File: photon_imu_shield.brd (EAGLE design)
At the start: 35.6 x 35.6 mm, 30 parts, among them U1 LSM9DS1

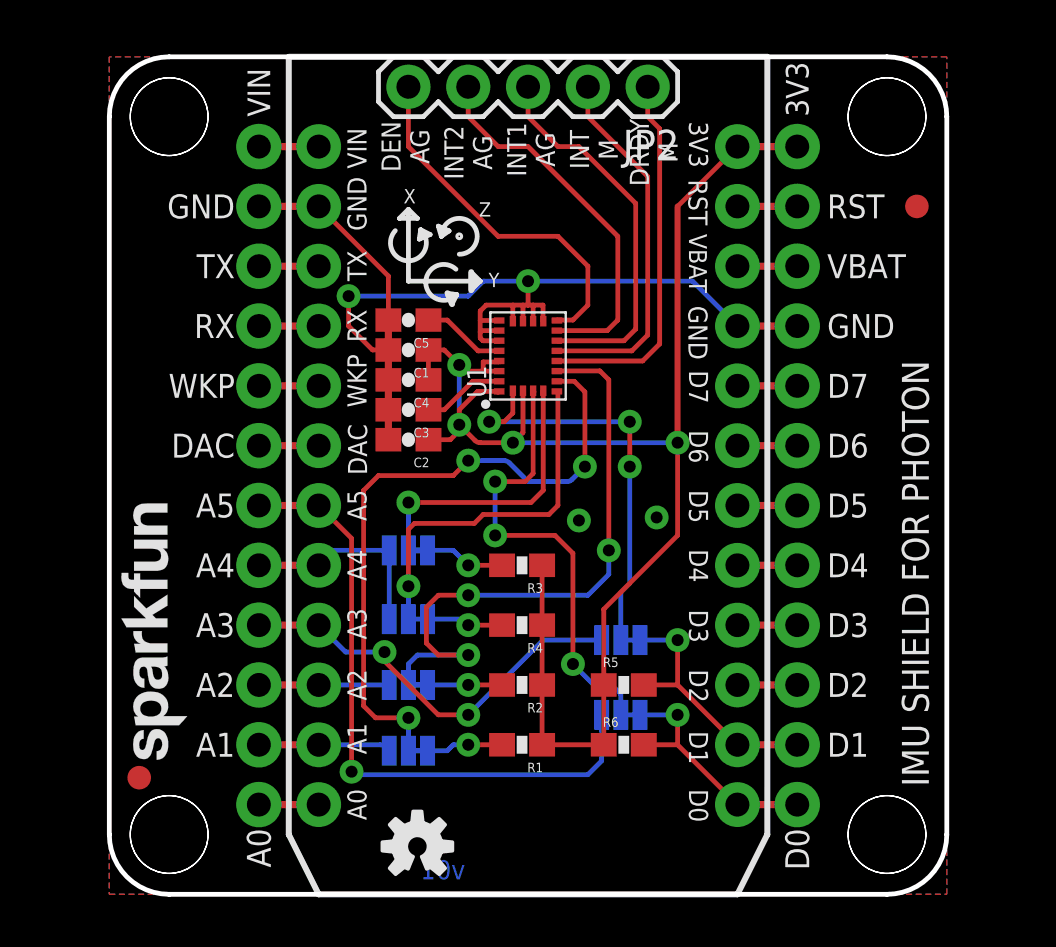
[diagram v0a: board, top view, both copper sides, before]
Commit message: Adding gap between Photon and pin breakouts.
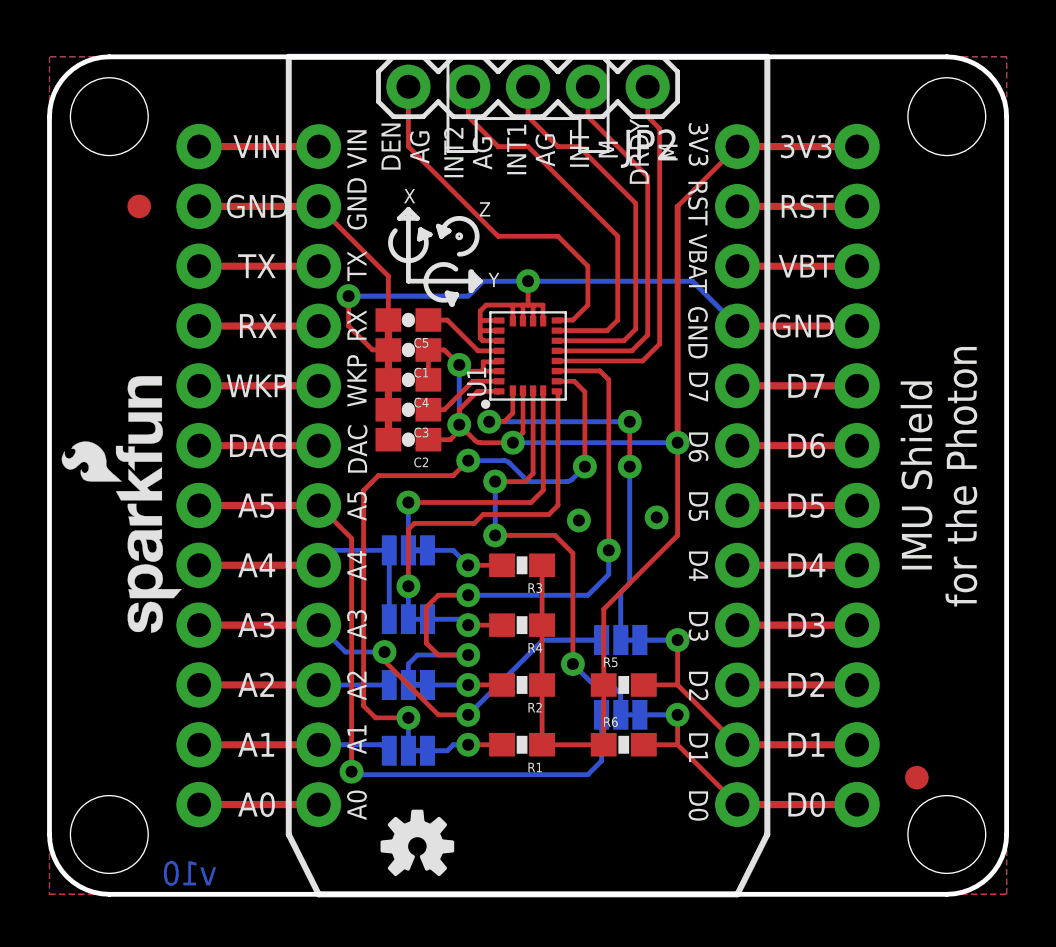
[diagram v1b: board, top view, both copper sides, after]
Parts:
- removed STANDOFF1, STANDOFF2, STANDOFF3, STANDOFF4: STAND-OFF, SparkFun-Electromechanical:STAND-OFF
- JP1: value SPARK_PHOTONTEMPLATE -> SPARK_PHOTONTEMPLATE_WIDE; device template_temp:SPARK_PHOTON_TEMPLATE -> template_temp:SPARK_PHOTON_TEMPLATE_WIDE
- LOGO1: value SFE_LOGO_NAME.1_INCH -> SFE_LOGO_NAME_FLAME.1_INCH; device SparkFun-Aesthetics:SFE_LOGO_NAME_.1 -> SparkFun-Aesthetics:SFE_LOGO_NAME_FLAME_.1
- moved FID1 33.0 mm to (1.27, 29.2)
- moved FID2 33.0 mm to (34.3, 4.95)
- moved FRAME1 30.6 mm to (-19.1, -10.2)
- moved LOGO1 5.50 mm to (3.17, 10.7)
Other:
- board size 35.6 x 35.6 mm -> 40.6 x 35.6 mm
- board text added: "IMU Shield for the Photon"
- board text added: "v10"
- board text removed: "IMU SHIELD FOR PHOTON"
- board text removed: "v01"
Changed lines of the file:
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@@
 <board>
 <plain>
-<text x="34.798" y="4.572" size="1.143" layer="21" font="vector" ratio="15" rot="R90">IMU SHIELD FOR PHOTON</text>
+<text x="36.83" y="17.78" size="1.27" layer="21" font="vector" ratio="15" rot="R90" align="bottom-center">IMU Shield
+for the Photon</text>
 <text x="17.526" y="14.732" size="0.8128" layer="22" font="vector" ratio="15" rot="MR270" align="bottom-center">SDO
 A/G</text>
@@
 <wire x1="13.16195" y1="27.819690625" x2="13.6227125" y2="28.014678125" width="0.2032" layer="21"/>
 <wire x1="13.6227125" y1="28.014678125" x2="13.220653125" y2="28.216984375" width="0.2032" layer="21"/>
-<wire x1="2.54" y1="35.56" x2="33.02" y2="35.56" width="0.2032" layer="20"/>
-<wire x1="33.02" y1="0" x2="2.54" y2="0" width="0.2032" layer="20"/>
-<text x="15.113" y="0.635" size="0.8128" layer="16" ratio="25" rot="MR0">v01</text>
-<wire x1="0" y1="2.54" x2="2.54" y2="0" width="0.2032" layer="20" curve="90"/>
-<wire x1="35.56" y1="2.54" x2="33.02" y2="0" width="0.2032" layer="20" curve="-90"/>
-<wire x1="35.56" y1="2.54" x2="35.56" y2="33.02" width="0.2032" layer="20"/>
-<wire x1="35.56" y1="33.02" x2="33.02" y2="35.56" width="0.2032" layer="20" curve="90"/>
-<wire x1="0" y1="2.54" x2="0" y2="33.02" width="0.2032" layer="20"/>
-<wire x1="0" y1="33.02" x2="2.54" y2="35.56" width="0.2032" layer="20" curve="-90"/>
-<text x="14.351" y="-40.767" size="1.778" layer="51" ratio="15">Ben Leduc-Mills</text>
+<wire x1="0" y1="35.56" x2="35.56" y2="35.56" width="0.2032" layer="20"/>
+<wire x1="35.56" y1="0" x2="0" y2="0" width="0.2032" layer="20"/>
+<text x="4.572" y="0.381" size="1.016" layer="16" ratio="15" rot="MR0">v10</text>
+<wire x1="-2.54" y1="2.54" x2="0" y2="0" width="0.2032" layer="20" curve="90"/>
+<wire x1="38.1" y1="2.54" x2="35.56" y2="0" width="0.2032" layer="20" curve="-90"/>
+<wire x1="38.1" y1="2.54" x2="38.1" y2="33.02" width="0.2032" layer="20"/>
+<wire x1="38.1" y1="33.02" x2="35.56" y2="35.56" width="0.2032" layer="20" curve="90"/>
+<wire x1="-2.54" y1="2.54" x2="-2.54" y2="33.02" width="0.2032" layer="20"/>
+<wire x1="-2.54" y1="33.02" x2="0" y2="35.56" width="0.2032" layer="20" curve="-90"/>
+<text x="11.811" y="-10.287" size="1.778" layer="51" ratio="15">Ben Leduc-Mills</text>
 <text x="11.303" y="31.623" size="0.8128" layer="22" font="vector" ratio="12" rot="MR90" align="bottom-center">DEN
 AG</text>
@@
 <dimension x1="2.54" y1="2.54" x2="0.889" y2="2.54" x3="1.7145" y3="-2.54" textsize="0.8128" textratio="15" layer="47" dtype="diameter" unit="inch" precision="3"/>
 <text x="0" y="-11.43" size="0.8128" layer="47" font="vector" ratio="15">Units in Inches</text>
-<text x="33.528" y="4.572" size="1.143" layer="22" font="vector" ratio="15" rot="MR90">IMU SHIELD FOR PHOTON</text>
+<text x="36.83" y="17.78" size="1.27" layer="22" font="vector" ratio="15" rot="MR270" align="bottom-center">IMU Shield
+for the Photon</text>
 </plain>
 <attributes>
@@
 </autorouter>
 <elements>
-<element name="JP1" library="template_temp" package="SPARK_PHOTON_TEMPLATE" value="SPARK_PHOTONTEMPLATE" x="7.62" y="0"/>
+<element name="JP1" library="template_temp" package="SPARK_PHOTON_TEMPLATE_WIDE" value="SPARK_PHOTONTEMPLATE_WIDE" x="7.62" y="0"/>
 <element name="U1" library="LSM9DS1_temp" package="LGA24-8X4" value="LSM9DS1" x="17.78" y="22.86" rot="R90">
 <attribute name="PROD_ID" value="IC-12536" x="17.78" y="22.86" size="1.778" layer="27" rot="R90" display="off"/>
@@
 <attribute name="PROD_ID" value="CAP-00867" x="12.7" y="24.384" size="1.778" layer="27" rot="R180" display="off"/>
 </element>
-<element name="FRAME1" library="SparkFun-Aesthetics" package="CREATIVE_COMMONS" value="FRAME-LETTER" x="-16.51" y="-40.64"/>
+<element name="FRAME1" library="SparkFun-Aesthetics" package="CREATIVE_COMMONS" value="FRAME-LETTER" x="-19.05" y="-10.16"/>
 <element name="R1" library="SparkFun-Resistors" package="0603-RES" value="10K" x="17.526" y="6.35" rot="R180">
 <attribute name="PROD_ID" value="RES-00824" x="17.526" y="6.35" size="1.778" layer="27" rot="R180" display="off"/>
@@
 <element name="SJ8" library="SparkFun-Passives" package="PAD-JUMPER-3-2OF3_NC_BY_TRACE_YES_SILK_FULL_BOX" value="" x="21.717" y="7.62" rot="MR180"/>
 <element name="U$5" library="SparkFun-Aesthetics" package="SFE_LOGO_NAME_FLAME_.1" value="" x="17.653" y="18.542" rot="MR90"/>
-<element name="FID1" library="SparkFun-Aesthetics" package="FIDUCIAL-1X2" value="FIDUCIAL1X2" x="34.29" y="29.21"/>
-<element name="FID2" library="SparkFun-Aesthetics" package="FIDUCIAL-1X2" value="FIDUCIAL1X2" x="1.27" y="4.953"/>
-<element name="STANDOFF1" library="SparkFun-Electromechanical" package="STAND-OFF" value="STAND-OFF" x="33.02" y="33.02"/>
-<element name="STANDOFF2" library="SparkFun-Electromechanical" package="STAND-OFF" value="STAND-OFF" x="2.54" y="33.02"/>
-<element name="STANDOFF3" library="SparkFun-Electromechanical" package="STAND-OFF" value="STAND-OFF" x="2.54" y="2.54"/>
-<element name="STANDOFF4" library="SparkFun-Electromechanical" package="STAND-OFF" value="STAND-OFF" x="33.02" y="2.54"/>
-<element name="LOGO1" library="SparkFun-Aesthetics" package="SFE_LOGO_NAME_.1" value="SFE_LOGO_NAME.1_INCH" x="3.81" y="5.207" rot="R90"/>
+<element name="FID1" library="SparkFun-Aesthetics" package="FIDUCIAL-1X2" value="FIDUCIAL1X2" x="1.27" y="29.21"/>
+<element name="FID2" library="SparkFun-Aesthetics" package="FIDUCIAL-1X2" value="FIDUCIAL1X2" x="34.29" y="4.953"/>
 <element name="LOGO2" library="SparkFun-Aesthetics" package="OSHW-LOGO-S" value="OSHW-LOGOS" x="13.081" y="2.032"/>
 <element name="JP2" library="SparkFun-Connectors" package="1X05" value="" x="22.86" y="34.29" rot="R180"/>
+<element name="LOGO1" library="SparkFun-Aesthetics" package="SFE_LOGO_NAME_FLAME_.1" value="SFE_LOGO_NAME_FLAME.1_INCH" x="3.175" y="10.668" rot="R90"/>
 </elements>
 <signals>
@@
 <contactref element="JP1" pad="GND@0"/>
 <polygon width="0.254" layer="1" isolate="0.3048">
-<vertex x="0" y="0"/>
-<vertex x="35.56" y="0"/>
-<vertex x="35.56" y="35.56"/>
-<vertex x="0" y="35.56"/>
+<vertex x="-2.54" y="0"/>
+<vertex x="38.1" y="0"/>
+<vertex x="38.1" y="35.56"/>
+<vertex x="-2.54" y="35.56"/>
 </polygon>
 <polygon width="0.254" layer="16" isolate="0.3048">
-<vertex x="0" y="0"/>
-<vertex x="35.56" y="0"/>
-<vertex x="35.56" y="35.56"/>
-<vertex x="0" y="35.56"/>
+<vertex x="-2.54" y="0"/>
+<vertex x="38.1" y="0"/>
+<vertex x="38.1" y="35.56"/>
+<vertex x="-2.54" y="35.56"/>
 </polygon>
 <wire x1="26.67" y1="24.13" x2="24.765" y2="26.035" width="0.2032" layer="16"/>
